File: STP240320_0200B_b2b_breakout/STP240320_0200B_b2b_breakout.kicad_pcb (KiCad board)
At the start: 2 copper layers, 35.6 x 59.2 mm, 18 parts, among them J1 Micro_SD_Card_Det_Hirose_DM3AT, J2 Conn_01x11, Q1 BSS138, U1 74HC4050D, U2 AP2112K-3.3, U3 LM809M3X-2.93

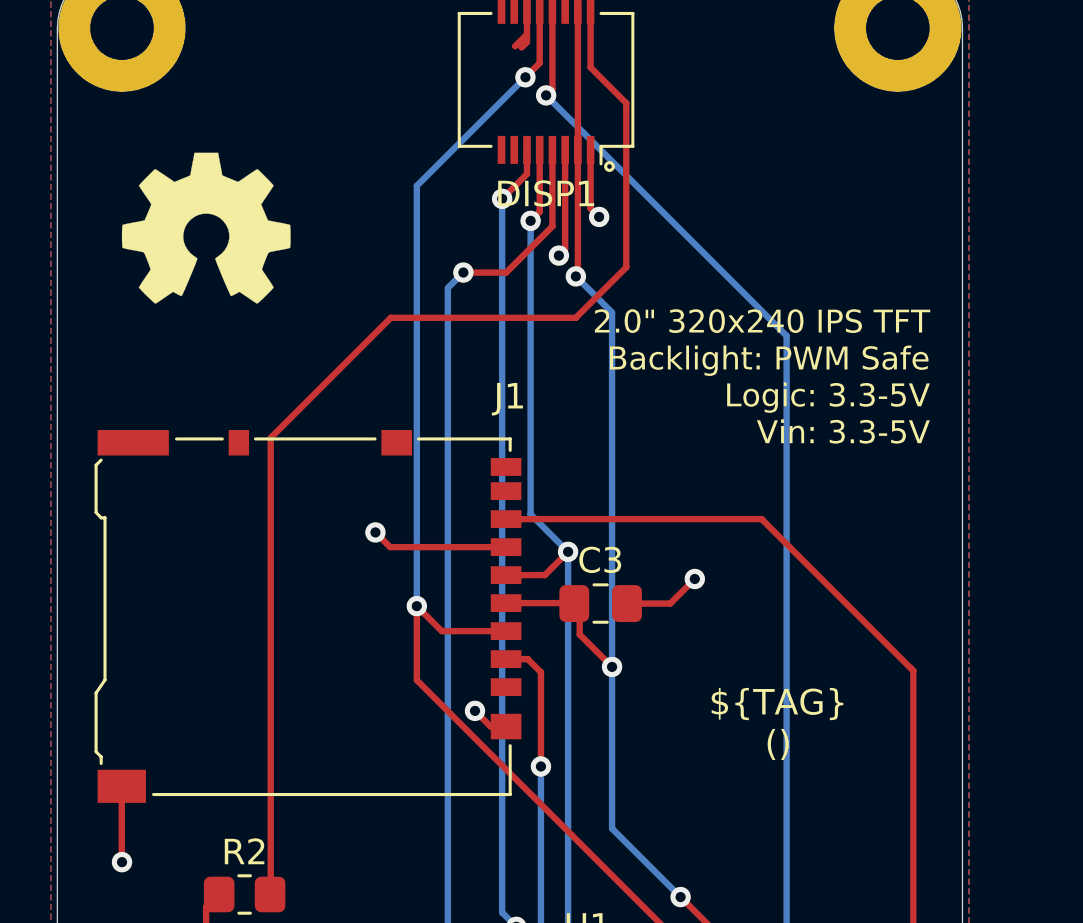
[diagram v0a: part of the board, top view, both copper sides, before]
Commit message: all: cleanup revision info
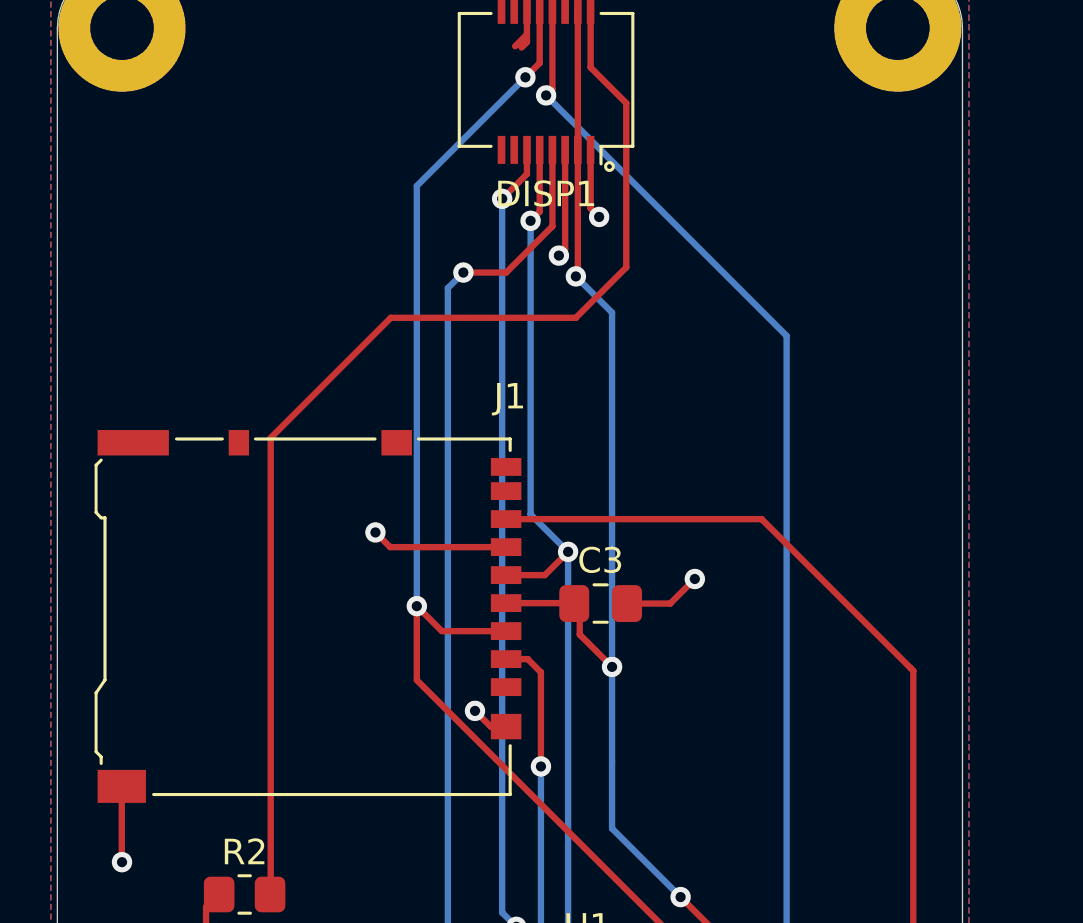
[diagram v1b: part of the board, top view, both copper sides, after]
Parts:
- LOGO1: footprint Symbol:OSHW-Symbol_6.7x6mm_SilkScreen -> Gigahawk:OSHW-Logo2_9.8x8mm_Mask
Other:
- board text added: "${TAG} (${HASH})"
- board text added: "2.0{dblquote} 320x240 IPS TFT Backlight: PWM Safe Logic: 3.3-5V Vin: 3.3-5V"
- board text removed: "${TAG} (${REVISION})"
- board text removed: "2.0" 320x240 IPS TFT Backlight: PWM Safe Logic: 3.3-5V Vin: 3.3-5V"

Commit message: breakout: add date to silkscreen
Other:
- board text added: "${DATE}"
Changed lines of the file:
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@@
+    (effects (font (size 1 1) (thickness 0.15)) (justify mirror))
+  )
+  (gr_text "${DATE}" (at 18.2 17.4) (layer "B.SilkS")
     (effects (font (size 1 1) (thickness 0.15)) (justify mirror))
   )
